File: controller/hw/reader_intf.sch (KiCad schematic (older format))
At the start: 27 parts, among them P402 Wago_233-502, P403 Wago_233-502, Q402 IRLML6402, U403 ROE-0505S, U404 HCPL-0601-500E, U405 HCPL-0601-500E, U406 Cosmo_1010-817, U407 SN75176BDR

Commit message: Compilability using embc lm4f, fixes to TX_EN switching
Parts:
- C301, C406: symbol Jamicon_220uF_25V -> capacitors:Jamicon_220uF_25V
- C407, C408, C409, C410, C411: symbol C -> simple:C
- F402: symbol FUSE -> templates:FUSE
- P402, P403: symbol Wago_233-502 -> connectors:Wago_233-502
- Q402: symbol IRLML6402 -> transistors:IRLML6402
- R401, R402, R403, R404, R405, R406, R407, R408, R409, R410, R411: symbol R -> simple:R
- U403: symbol ROE-0505S -> power:ROE-0505S
- U404, U405: symbol HCPL-0601-500E -> opto:HCPL-0601-500E
- U406: symbol Cosmo_1010-817 -> opto:Cosmo_1010-817
- U407: symbol SN75176BDR -> ic:SN75176BDR
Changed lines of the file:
@@
-EESchema Schematic File Version 2
-LIBS:74xx
-LIBS:boards
-LIBS:buttons
-LIBS:capacitors
-LIBS:connectors
-LIBS:cpu
-LIBS:discrete
-LIBS:drivers
-LIBS:ic
-LIBS:mspower
-LIBS:opto
-LIBS:passives
-LIBS:power
-LIBS:relay
-LIBS:rf
-LIBS:simple
-LIBS:transistors
-LIBS:templates
+EESchema Schematic File Version 4
 LIBS:dvernik-cache
 EELAYER 26 0
@@
 $EndDescr
 $Comp
-L ROE-0505S U403
+L power:ROE-0505S U403
 U 1 1 5917718B
 P 5300 1300
@@
 $EndComp
 $Comp
-L R R402
+L simple:R R402
 U 1 1 591771B1
 P 4150 2000
@@
 $EndComp
 $Comp
-L R R406
+L simple:R R406
 U 1 1 591771B8
 P 6350 2100
@@
 $EndComp
 $Comp
-L R R405
+L simple:R R405
 U 1 1 591771C6
 P 5900 2600
@@
 $EndComp
 $Comp
-L R R404
+L simple:R R404
 U 1 1 591771CD
 P 4700 3250
@@
 $EndComp
 $Comp
-L GND #PWR034
+L mspower:GND #PWR034
 U 1 1 591771F0
 P 5000 2400
@@
 $EndComp
 $Comp
-L GNDA #PWR035
+L mspower:GNDA #PWR035
 U 1 1 5917720A
 P 5850 3250
@@
 $EndComp
 $Comp
-L GNDA #PWR036
+L mspower:GNDA #PWR036
 U 1 1 5917721C
 P 5800 1550
@@
 CPU_TX
 $Comp
-L +5VA #PWR037
+L mspower:+5VA #PWR037
 U 1 1 5917722F
 P 6350 1100
@@
 $EndComp
 $Comp
-L C C407
+L simple:C C407
 U 1 1 5917723B
 P 4650 1300
@@
 $EndComp
 $Comp
-L C C408
+L simple:C C408
 U 1 1 59177249
 P 5800 1300
@@
 UNSAFE_TX
 $Comp
-L HCPL-0601-500E U404
+L opto:HCPL-0601-500E U404
 U 1 1 5917725E
 P 5300 2250
@@
 $EndComp
 $Comp
-L HCPL-0601-500E U405
+L opto:HCPL-0601-500E U405
 U 1 1 59177265
 P 5300 3150
@@
 Connection ~ 3900 1100
 $Comp
-L SN75176BDR U407
+L ic:SN75176BDR U407
 U 1 1 59177EF3
 P 8250 2800
@@
 	6150 1100 6150 4650
 $Comp
-L C C409
+L simple:C C409
 U 1 1 5917845D
 P 6350 3450
@@
 $EndComp
 $Comp
-L GNDA #PWR038
+L mspower:GNDA #PWR038
 U 1 1 591784F4
 P 6500 3600
@@
 Connection ~ 6150 2900
 $Comp
-L C C411
+L simple:C C411
 U 1 1 5917860E
 P 8450 1800
@@
 Connection ~ 8250 1400
 $Comp
-L GNDA #PWR039
+L mspower:GNDA #PWR039
 U 1 1 59178885
 P 8450 1950
@@
 	5700 1500 6600 1500
 $Comp
-L GNDA #PWR040
+L mspower:GNDA #PWR040
 U 1 1 591789EC
 P 8250 3100
@@
 $EndComp
 $Comp
-L Wago_233-502 P402
+L connectors:Wago_233-502 P402
 U 1 1 59178A7E
 P 9200 2800
@@
 	8800 2900 8650 2900
 $Comp
-L Cosmo_1010-817 U406
+L opto:Cosmo_1010-817 U406
 U 1 1 59178DD0
 P 5300 4750
@@
 	7800 4850 5600 4850
 $Comp
-L C C410
+L simple:C C410
 U 1 1 59178F22
 P 6350 4350
@@
 $EndComp
 $Comp
-L GNDA #PWR041
+L mspower:GNDA #PWR041
 U 1 1 59179160
 P 6500 4450
@@
 Connection ~ 6150 4350
 $Comp
-L GNDA #PWR042
+L mspower:GNDA #PWR042
 U 1 1 591794D3
 P 7350 3600
@@
 $EndComp
 $Comp
-L R R407
+L simple:R R407
 U 1 1 5917952C
 P 7550 3500
@@
 Connection ~ 7800 3500
 $Comp
-L R R403
+L simple:R R403
 U 1 1 5917984B
 P 4750 4850
@@
 RS485
 $Comp
-L Wago_233-502 P403
+L connectors:Wago_233-502 P403
 U 1 1 5917A251
 P 10100 1150
@@
 Connection ~ 8250 1100
 $Comp
-L GNDA #PWR043
+L mspower:GNDA #PWR043
 U 1 1 5917A355
 P 9000 1400
@@
 	9900 1200 9000 1200
 $Comp
-L FUSE F402
+L templates:FUSE F402
 U 1 1 5917A6EB
 P 9150 1100
@@
 	1900 1100 3050 1100
 $Comp
-L R R401
+L simple:R R401
 U 1 1 591869D7
 P 3000 1400
@@
 	3250 1900 2750 1900
 $Comp
-L IRLML6402 Q402
+L transistors:IRLML6402 Q402
 U 1 1 59186E57
 P 3250 1200
@@
 ~READER_ON
 $Comp
-L R R410
+L simple:R R410
 U 1 1 5918D8C0
 P 5900 2350
@@
 $EndComp
 $Comp
-L R R411
+L simple:R R411
 U 1 1 5918D906
 P 6750 2100
@@
 Connection ~ 5650 2350
 $Comp
-L R R408
+L simple:R R408
 U 1 1 5918DF82
 P 4150 2200
@@
 Connection ~ 4450 2200
 $Comp
-L R R409
+L simple:R R409
 U 1 1 5918E10D
 P 4700 3500
@@
 Power for reader
 $Comp
-L Jamicon_220uF_25V C406
+L capacitors:Jamicon_220uF_25V C406
 U 1 1 59172B3A
 P 2300 1300
@@
 $EndComp
 $Comp
-L Jamicon_220uF_25V C301
+L capacitors:Jamicon_220uF_25V C301
 U 1 1 59180D99
 P 6600 1300

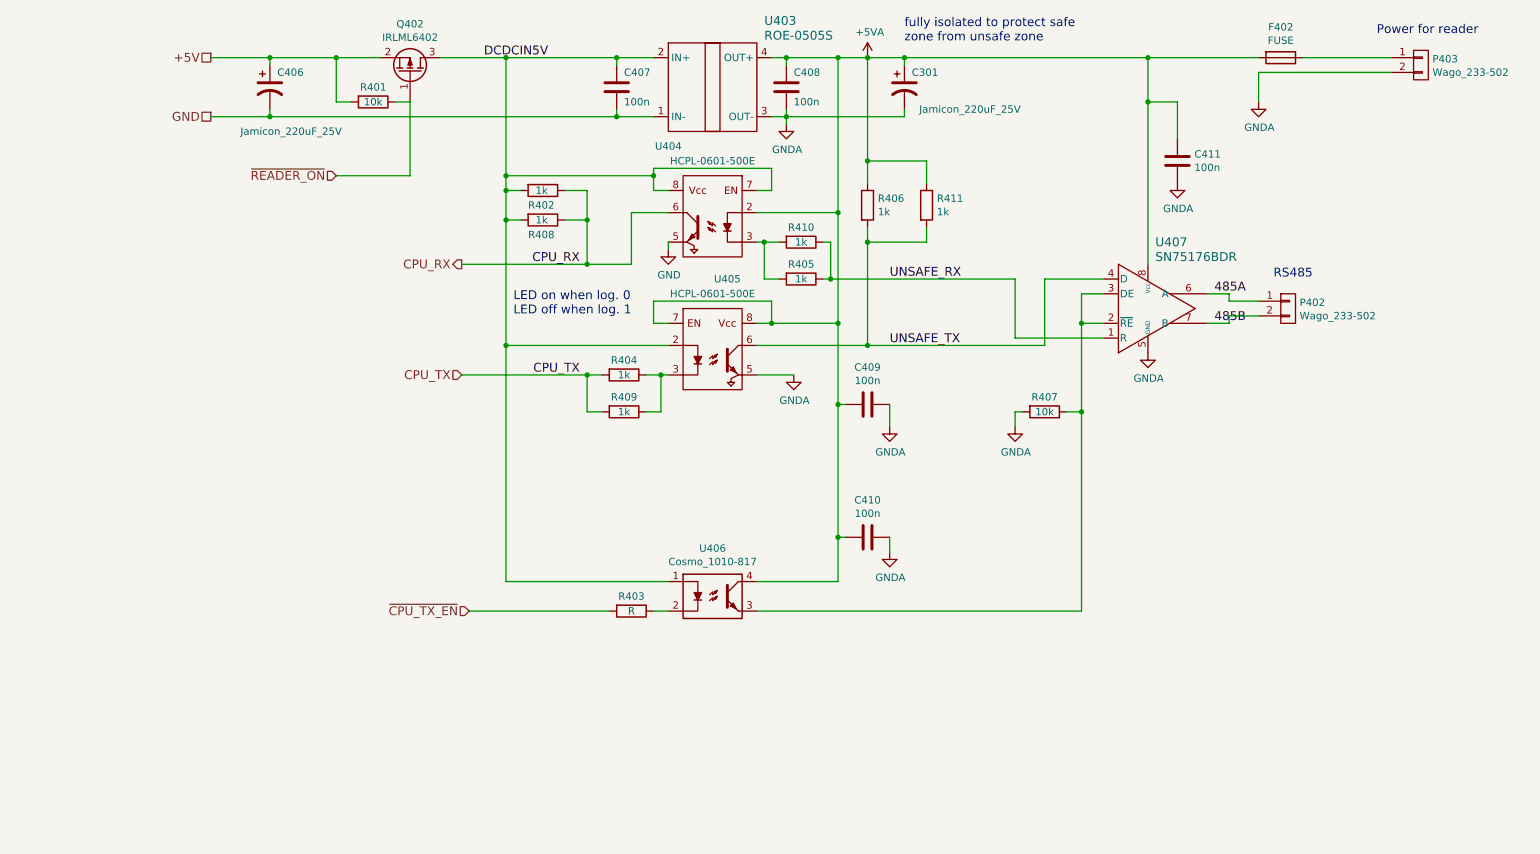
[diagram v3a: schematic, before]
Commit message: Fix serious hw bug (5V level on 3.3V tolerant RX/TX on ctrl board)
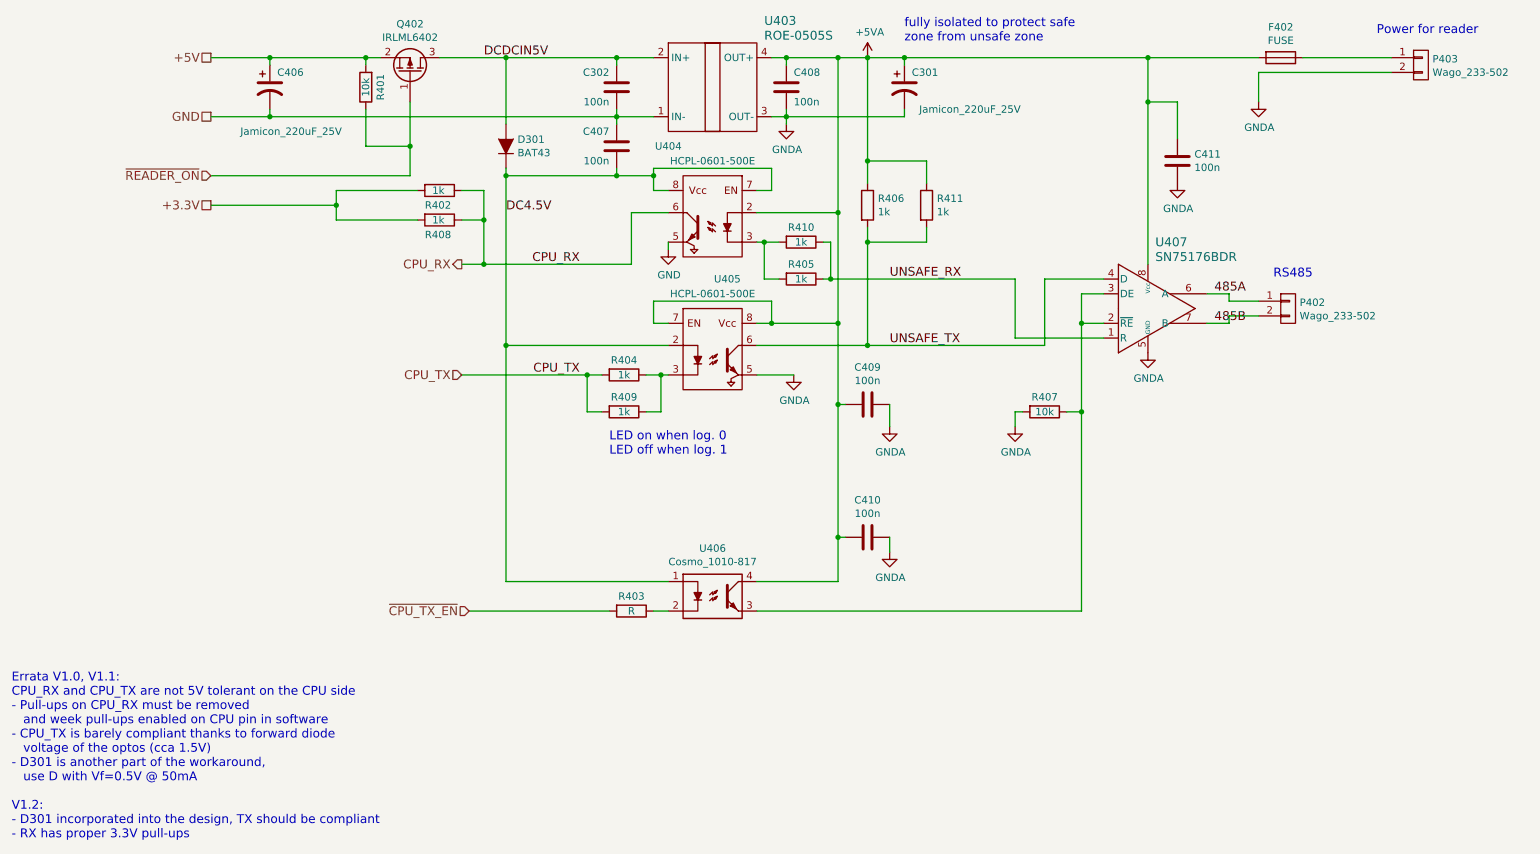
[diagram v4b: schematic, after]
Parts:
- added C302: 100n, smd-handsolder:C_1206_HandSoldering, symbol simple:C
- added D301: BAT43, smd-handsolder:Diode_1206_HandSoldering, symbol simple:D
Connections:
- net DCDCIN5V: now also C302.1, D301.2 (A); no longer C407.1, R402.2, R408.2, U404.7 (EN), U404.8 (Vcc), U405.2, U406.1
- net GND: now also C407.1, C302.2; no longer C407.2
- new net +3.3V: R402.2, R408.2
- new net DC4.5V: C407.2, D301.1 (K), U404.7 (EN), U404.8 (Vcc), U405.2, U406.1
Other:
- note added: "Errata V1.0, V1.1:\nCPU_RX and CPU_TX are not 5V tolerant on the CPU side\n- Pull-ups on CPU_RX must be removed\n and week pull-ups enabled on CPU pin in software\n- CPU_TX is barely compliant thanks to forward diode\n voltage of the optos (cca 1.5V)\n- D301 is another part of the workaround,\n use D with Vf=0.5V @ 50mA\n\nV1.2:\n- D301 incorporated into the design, TX should be compliant\n- RX h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"
- moved on the sheet: C407, R401, R402, R408

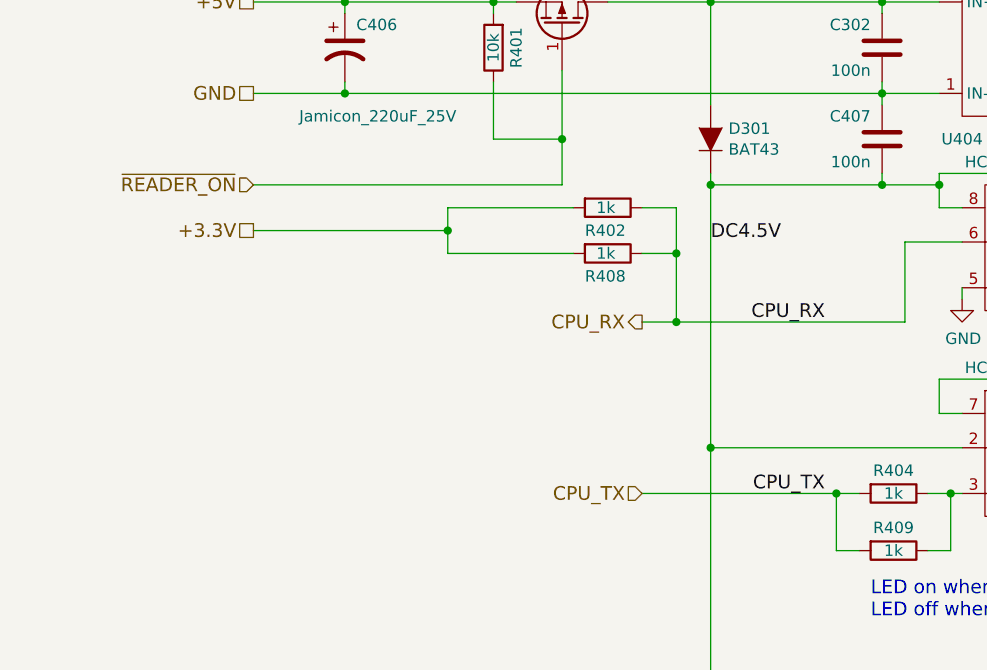
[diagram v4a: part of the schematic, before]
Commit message: Fix controller issues with 3.3V CPU interfacing 5V logic
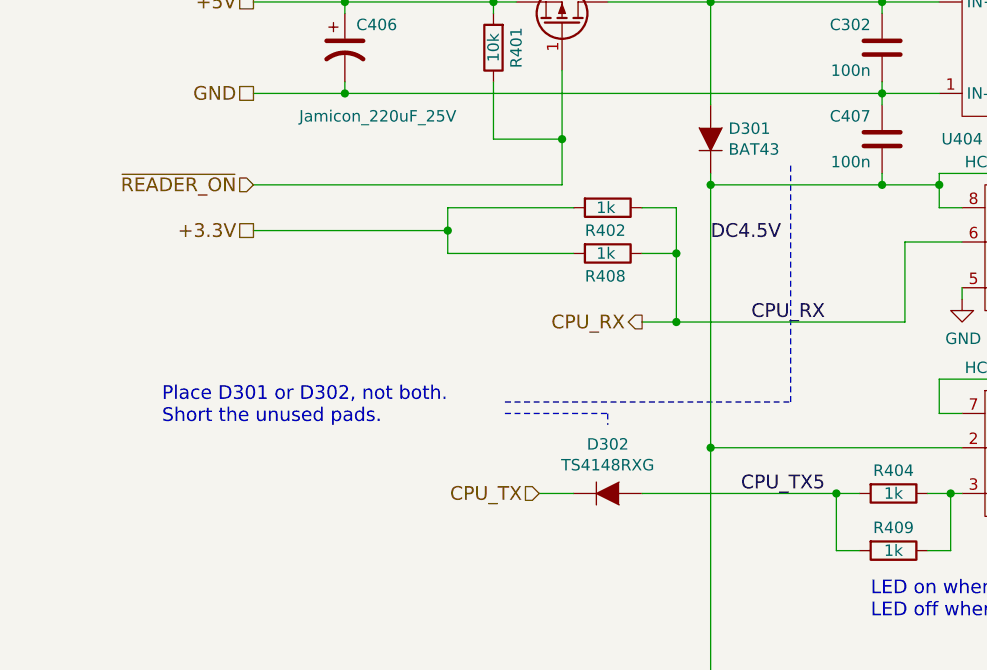
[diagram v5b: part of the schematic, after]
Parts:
- added D302: TS4148RXG, smd-handsolder:Diode_1206_HandSoldering, symbol simple:TS4148RXG
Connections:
- net CPU_TX: now also D302.1 (K); no longer R404.2, R409.2
- new net CPU_TX5: D302.2 (A), R404.2, R409.2
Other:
- note added: "Place D301 or D302, not both.\nShort the unused pads."
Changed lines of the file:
@@
 CPU_RX
 Text Label 4400 3250 2    60   ~ 0
-CPU_TX
+CPU_TX5
 $Comp
 L mspower:+5VA #PWR037
@@
 	1    0    0    -1
 $EndComp
-Text HLabel 3600 3250 0    60   Input ~ 0
+Text HLabel 3150 3250 0    60   Input ~ 0
 CPU_TX
 Text HLabel 3600 2500 0    60   Output ~ 0
@@
 	-1   0    0    -1
 $EndComp
+$Comp
+L simple:TS4148RXG D302
+U 1 1 5A34F7A3
+P 3450 3250
+F 0 "D302" H 3450 3465 50  0000 C CNN
+F 1 "TS4148RXG" H 3450 3374 50  0000 C CNN
+F 2 "smd-handsolder:Diode_1206_HandSoldering" H 3450 3250 60  0001 C CNN
+F 3 "" H 3450 3250 60  0000 C CNN
+	1    3450 3250
+	1    0    0    -1
+$EndComp
+Wire Wire Line
+	3150 3250 3300 3250
+Text Notes 1500 2950 0    60   ~ 0
+Place D301 or D302, not both.\nShort the unused pads.
+Wire Notes Line
+	3000 2900 3450 2900
+Wire Notes Line
+	3450 2900 3450 2950
+Wire Notes Line
+	3000 2850 4250 2850
+Wire Notes Line
+	4250 2850 4250 1800
 $EndSCHEMATC

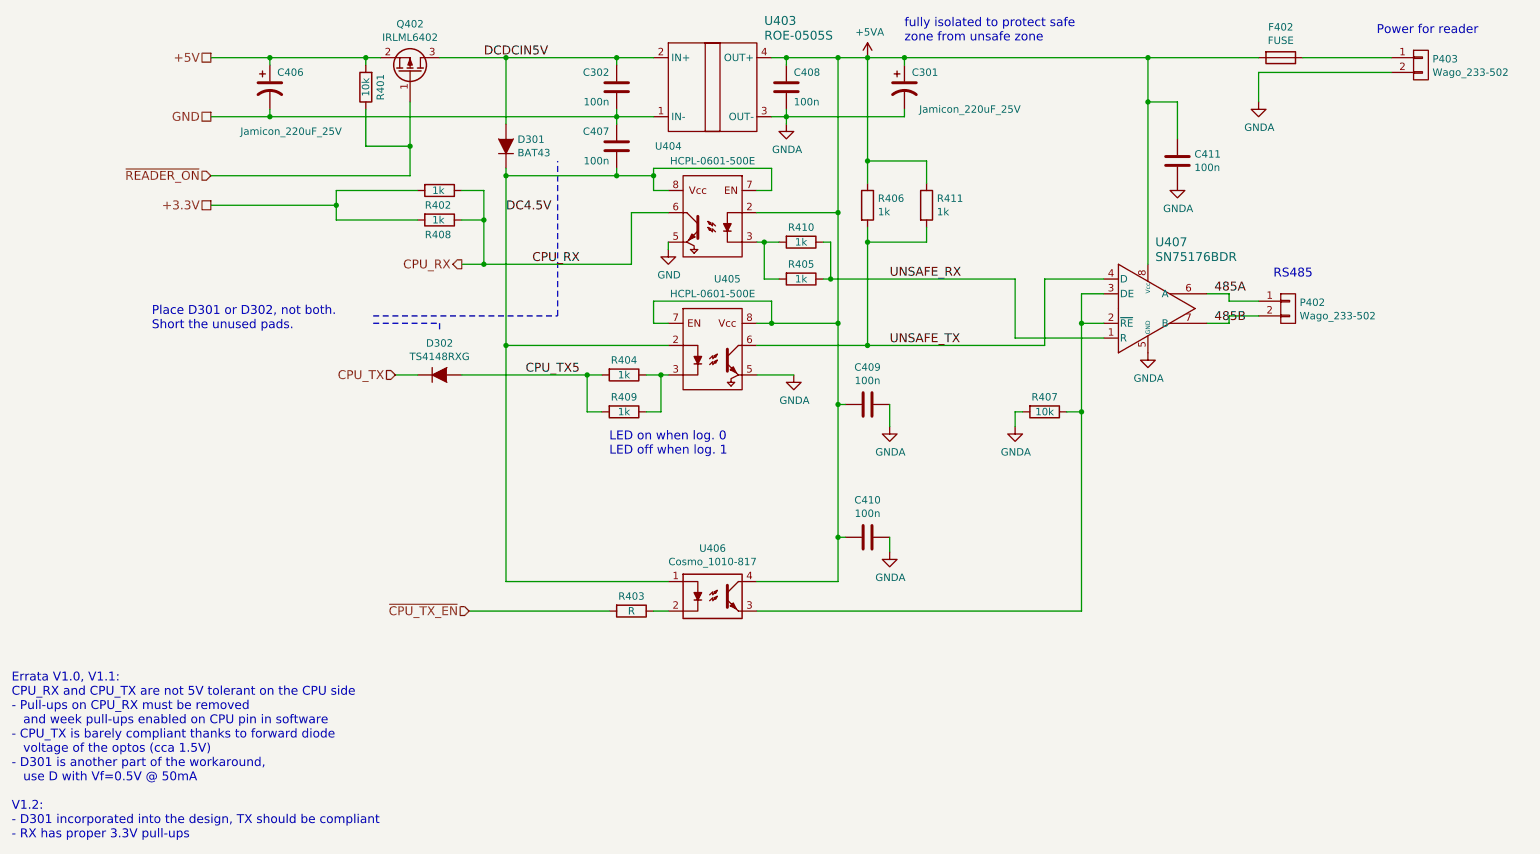
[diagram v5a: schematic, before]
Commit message: WIP Still working in 3.3 - 5V interface issues
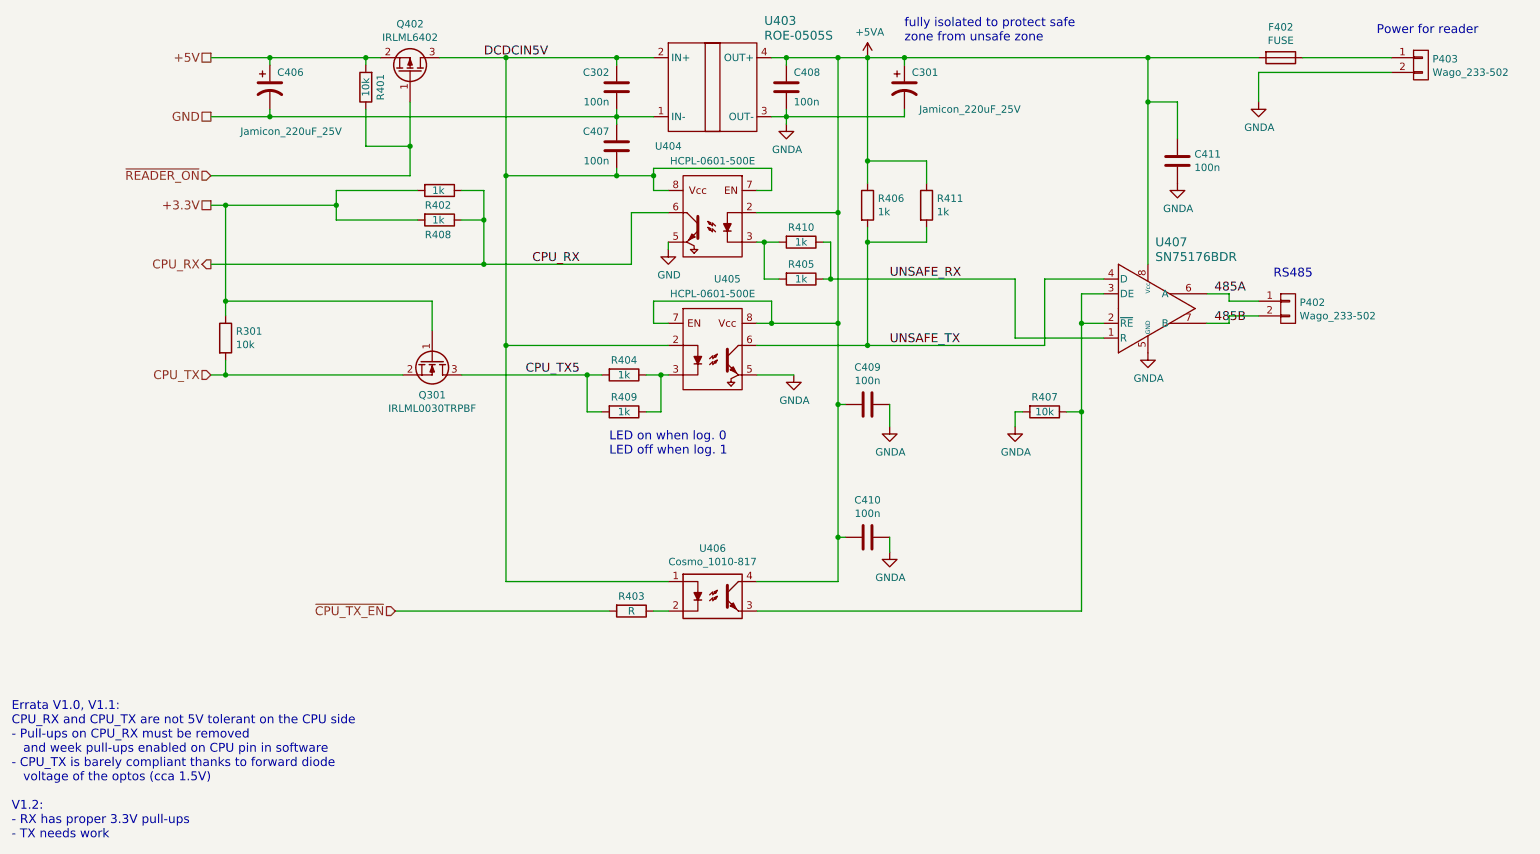
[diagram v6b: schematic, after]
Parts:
- removed D301: BAT43, smd-handsolder:Diode_1206_HandSoldering, symbol simple:D
- removed D302: TS4148RXG, smd-handsolder:Diode_1206_HandSoldering, symbol simple:TS4148RXG
- added Q301: IRLML0030TRPBF, smd-handsolder:SOT-23_HandSoldering, symbol transistors:IRLML0030TRPBF
- added R301: 10k, smd-handsolder:R_1206_HandSoldering, symbol simple:R
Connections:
- net DC4.5V is gone; now on net DCDCIN5V: C407.2, U404.7 (EN), U404.8 (Vcc), U405.2, U406.1
- net +3.3V: now also Q301.1 (G), R301.1
- net CPU_TX: now also Q301.2 (S), R301.2
- net CPU_TX5: now also Q301.3 (D)
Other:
- note added: "Errata V1.0, V1.1:\nCPU_RX and CPU_TX are not 5V tolerant on the CPU side\n- Pull-ups on CPU_RX must be removed\n and week pull-ups enabled on CPU pin in software\n- CPU_TX is barely compliant thanks to forward diode\n voltage of the optos (cca 1.5V)\n\nV1.2:\n- RX has proper 3.3V pull-ups\n- TX needs work"
- note removed: "Errata V1.0, V1.1:\nCPU_RX and CPU_TX are not 5V tolerant on the CPU side\n- Pull-ups on CPU_RX must be removed\n and week pull-ups enabled on CPU pin in software\n- CPU_TX is barely compliant thanks to forward diode\n voltage of the optos (cca 1.5V)\n- D301 is another part of the workaround,\n use D with Vf=0.5V @ 50mA\n\nV1.2:\n- D301 incorporated into the design, TX should be compliant\n- RX h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"
- note removed: "Place D301 or D302, not both.\nShort the unused pads."
